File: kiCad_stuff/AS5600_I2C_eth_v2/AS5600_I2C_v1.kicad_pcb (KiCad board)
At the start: 2 copper layers, 22 x 18.4 mm, 8 parts, among them J1 SCL GND +5V SDA, U1 AS5600_ASOM_vEth2

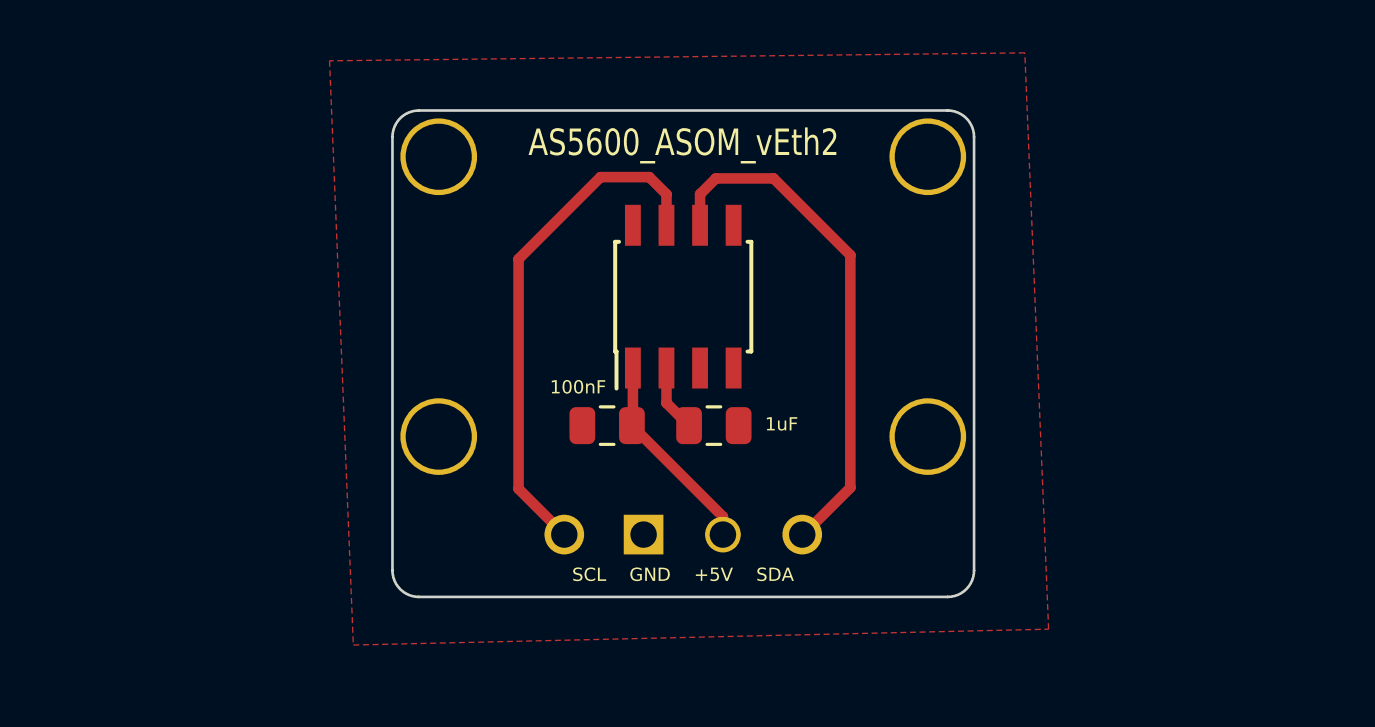
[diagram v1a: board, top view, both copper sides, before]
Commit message: Started designing PCB using ADC-to-I2C chip
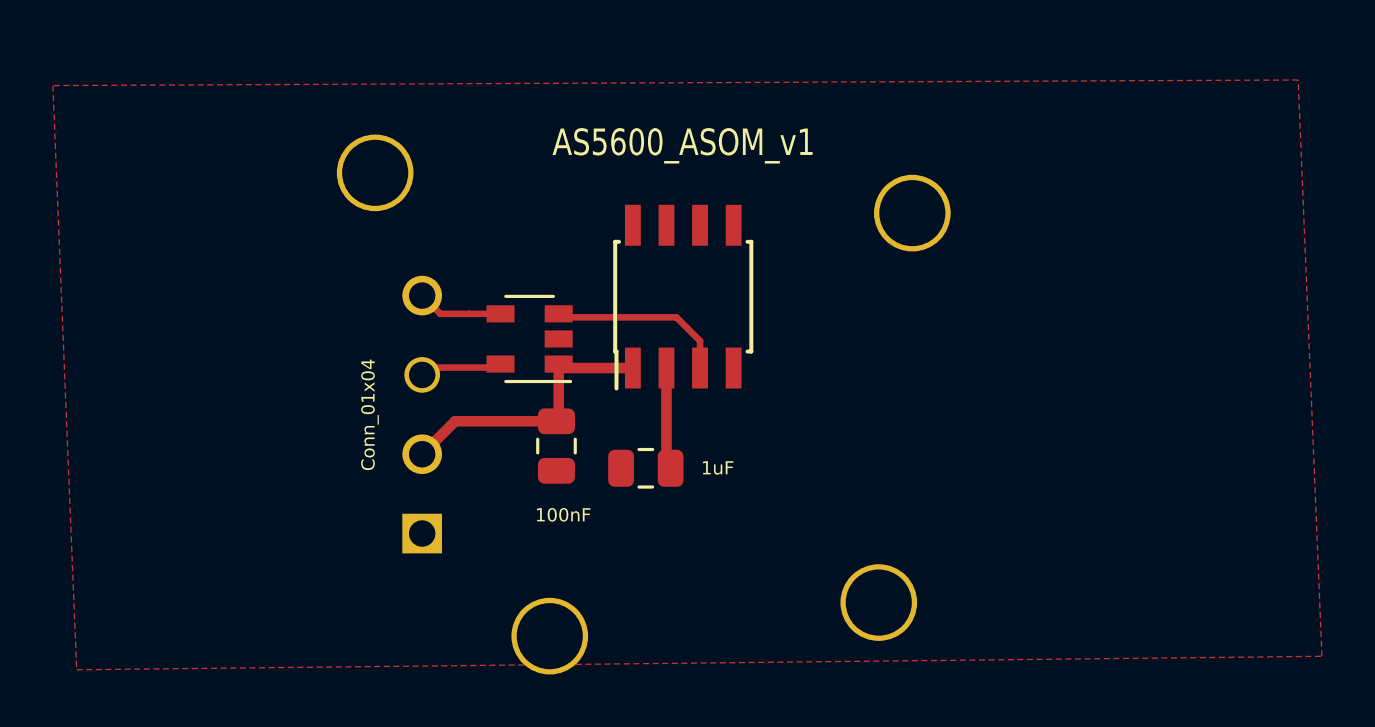
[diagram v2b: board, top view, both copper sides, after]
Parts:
- added U2: MCP3221, Package_TO_SOT_SMD:SOT-23-5, F.Cu at (162.7, 77.2)
- J1: value SCL GND +5V SDA -> Conn_01x04
- U1: value AS5600_ASOM_vEth2 -> AS5600_ASOM_v1
- moved J1 10.9 mm to (158.6, 80.1), turned to 90 degrees
- moved 2.5mm  8.64 mm to (163.4, 88.5)
- moved 2.5mm  6.55 mm to (175.9, 87.2)
- moved C2 3.04 mm to (167.1, 82.1), turned to 180 degrees
- moved 2.5mm  2.48 mm to (156.8, 70.9)
- moved 2.5mm  2.21 mm to (177.1, 72.5)
- moved C1 2.07 mm to (163.7, 81.3), turned to 270 degrees
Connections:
- J1 pad 1: SCL -> GND
- J1 pad 2: GND -> +5V
- J1 pad 3: +5V -> SCL
- U1 pad 3: Net-(U1-Pad3) -> ANALOG
- U1 pad 5: Net-(U1-Pad5) -> (no net)
- U1 pad 6: SDA -> (no net)
- U1 pad 7: SCL -> (no net)
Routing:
- net SDA: track 19.7 -> 3.25 mm
- net SCL: track 19.5 -> 3.13 mm
- net ANALOG: track 0.00 -> 6.74 mm
- net +5V: track 7.80 -> 11.5 mm
- net Net-(C2-Pad1): track 2.53 -> 3.86 mm
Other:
- board outline removed
- net class ANALOG added: clearance 0.3, trace_width 0.25, via_dia 0.8, via_drill 0.4
